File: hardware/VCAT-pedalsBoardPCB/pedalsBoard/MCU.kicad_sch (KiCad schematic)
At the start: 0 parts

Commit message: test
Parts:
- added D1: LED, LHRS_Special:RGB_LED, symbol Device:LED
- added D2, D3: LED, symbol Device:LED
- added R5, R7, R8: 1k, Resistor_SMD:R_0603_1608Metric, symbol Device:R
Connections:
- net 48PinMCU1/PB0: now also R5.1
- net 48PinMCU1/PB1: now also R7.1
- net 48PinMCU1/PB2: now also R8.1
- net GND: now also D1.1 (K), D2.1 (K), D3.1 (K)
- new net: D3.2 (A), R8.2
- new net: D1.2 (A), R5.2
- new net: D2.2 (A), R7.2
- no-connect marks 25 -> 21
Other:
- sheet 48PinMCU1 ports: added none; removed USB_DM, USB_DP

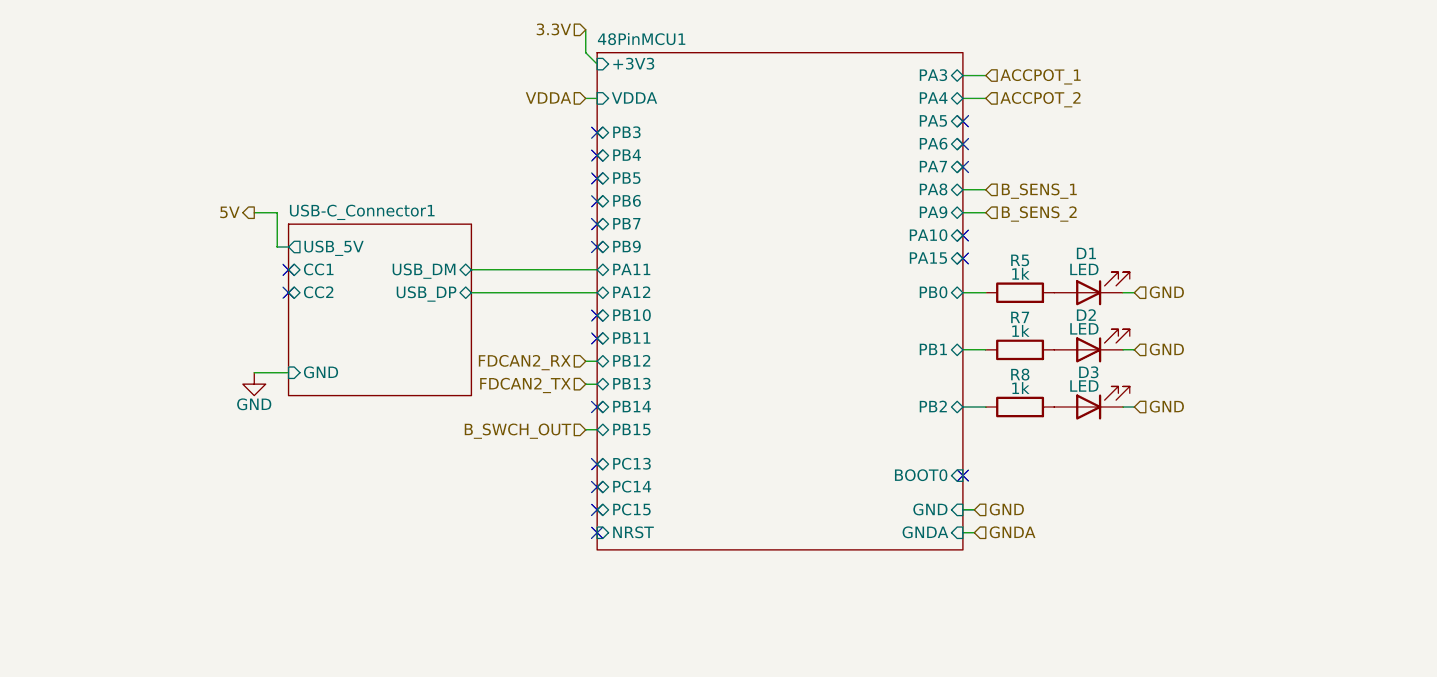
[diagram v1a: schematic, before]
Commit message: implemented review suggestions and added bus
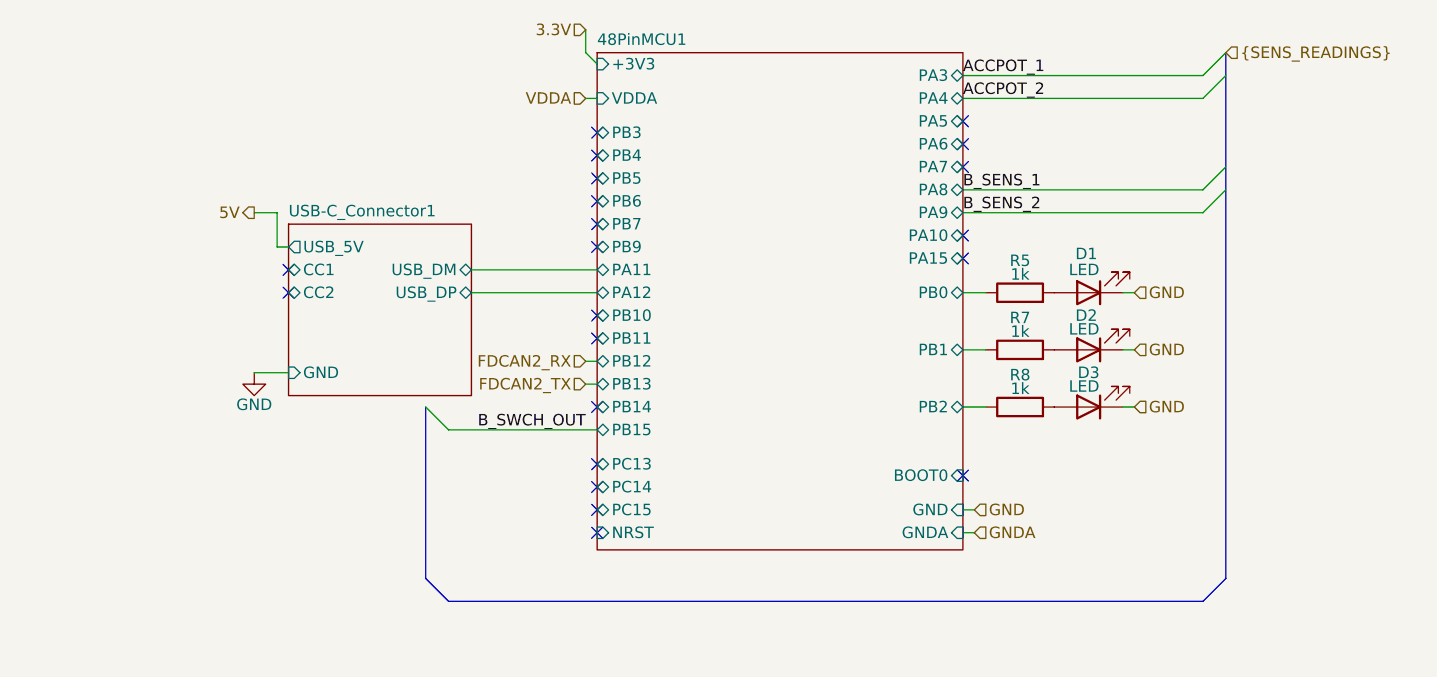
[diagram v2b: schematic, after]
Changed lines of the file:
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@@
 		(at 44.45 64.77)
 	)
-	(wire
-		(pts
-			(xy 119.38 43.18) (xy 121.92 43.18)
+	(bus_entry
+		(at 148.59 53.34)
+		(size -2.54 2.54)
+		(stroke
+			(width 0)
+			(type default)
+		)
+	)
+	(bus_entry
+		(at 59.69 77.47)
+		(size 2.54 2.54)
+		(stroke
+			(width 0)
+			(type default)
+		)
+	)
+	(bus_entry
+		(at 148.59 50.8)
+		(size -2.54 2.54)
+		(stroke
+			(width 0)
+			(type default)
+		)
+	)
+	(bus_entry
+		(at 148.59 38.1)
+		(size -2.54 2.54)
+		(stroke
+			(width 0)
+			(type default)
+		)
+	)
+	(bus_entry
+		(at 148.59 40.64)
+		(size -2.54 2.54)
+		(stroke
+			(width 0)
+			(type default)
+		)
+	)
+	(bus
+		(pts
+			(xy 59.69 77.47) (xy 59.69 96.52)
+		)
+		(stroke
+			(width 0)
+			(type default)
+		)
+	)
+	(wire
+		(pts
+			(xy 119.38 53.34) (xy 146.05 53.34)
+		)
+		(stroke
+			(width 0)
+			(type default)
+		)
+	)
+	(bus
+		(pts
+			(xy 148.59 38.1) (xy 148.59 96.52)
 		)
 		(stroke
@@
 	(wire
 		(pts
+			(xy 119.38 40.64) (xy 146.05 40.64)
+		)
+		(stroke
+			(width 0)
+			(type default)
+		)
+	)
+	(wire
+		(pts
 			(xy 119.38 71.12) (xy 121.92 71.12)
 		)
@@
 	(wire
 		(pts
-			(xy 119.38 40.64) (xy 121.92 40.64)
-		)
-		(stroke
-			(width 0)
-			(type default)
-		)
-	)
-	(wire
-		(pts
-			(xy 77.47 80.01) (xy 78.74 80.01)
+			(xy 119.38 43.18) (xy 146.05 43.18)
 		)
 		(stroke
@@
 		)
 	)
+	(bus
+		(pts
+			(xy 59.69 96.52) (xy 62.23 99.06)
+		)
+		(stroke
+			(width 0)
+			(type default)
+		)
+	)
 	(wire
 		(pts
@@
 		)
 	)
+	(bus
+		(pts
+			(xy 62.23 99.06) (xy 146.05 99.06)
+		)
+		(stroke
+			(width 0)
+			(type default)
+		)
+	)
 	(wire
 		(pts
@@
 	(wire
 		(pts
-			(xy 119.38 53.34) (xy 121.92 53.34)
-		)
-		(stroke
-			(width 0)
-			(type default)
-		)
-	)
-	(wire
-		(pts
 			(xy 137.16 64.77) (xy 138.43 64.77)
 		)
@@
 	(wire
 		(pts
-			(xy 119.38 55.88) (xy 121.92 55.88)
-		)
-		(stroke
-			(width 0)
-			(type default)
+			(xy 62.23 80.01) (xy 78.74 80.01)
+		)
+		(stroke
+			(width 0)
+			(type default)
+		)
+	)
+	(wire
+		(pts
+			(xy 119.38 55.88) (xy 146.05 55.88)
+		)
+		(stroke
+			(width 0)
+			(type default)
+		)
+	)
+	(bus
+		(pts
+			(xy 146.05 99.06) (xy 148.59 96.52)
+		)
+		(stroke
+			(width 0)
+			(type default)
+		)
+	)
+	(label "B_SENS_2"
+		(at 119.38 55.88 0)
+		(effects
+			(font
+				(size 1.27 1.27)
+			)
+			(justify left bottom)
+		)
+	)
+	(label "ACCPOT_1"
+		(at 119.38 40.64 0)
+		(effects
+			(font
+				(size 1.27 1.27)
+			)
+			(justify left bottom)
+		)
+	)
+	(label "ACCPOT_2"
+		(at 119.38 43.18 0)
+		(effects
+			(font
+				(size 1.27 1.27)
+			)
+			(justify left bottom)
+		)
+	)
+	(label "B_SWCH_OUT"
+		(at 77.47 80.01 180)
+		(effects
+			(font
+				(size 1.27 1.27)
+			)
+			(justify right bottom)
+		)
+	)
+	(label "B_SENS_1"
+		(at 119.38 53.34 0)
+		(effects
+			(font
+				(size 1.27 1.27)
+			)
+			(justify left bottom)
 		)
 	)
@@
 			)
 			(justify left)
-		)
-	)
-	(hierarchical_label "B_SWCH_OUT"
-		(shape input)
-		(at 77.47 80.01 180)
-		(effects
-			(font
-				(size 1.27 1.27)
-			)
-			(justify right)
 		)
 	)
@@
 		)
 	)
-	(hierarchical_label "B_SENS_2"
-		(shape input)
-		(at 121.92 55.88 0)
+	(hierarchical_label "FDCAN2_TX"
+		(shape input)
+		(at 77.47 74.93 180)
+		(effects
+			(font
+				(size 1.27 1.27)
+			)
+			(justify right)
+		)
+	)
+	(hierarchical_label "GND"
+		(shape input)
+		(at 138.43 77.47 0)
 		(effects
 			(font
@@
 		)
 	)
-	(hierarchical_label "B_SENS_1"
-		(shape input)
-		(at 121.92 53.34 0)
+	(hierarchical_label "GND"
+		(shape input)
+		(at 138.43 64.77 0)
 		(effects
 			(font
@@
 		)
 	)
-	(hierarchical_label "FDCAN2_TX"
-		(shape input)
-		(at 77.47 74.93 180)
-		(effects
-			(font
-				(size 1.27 1.27)
-			)
-			(justify right)
-		)
-	)
-	(hierarchical_label "ACCPOT_2"
-		(shape input)
-		(at 121.92 43.18 0)
-		(effects
-			(font
-				(size 1.27 1.27)
-			)
-			(justify left)
-		)
-	)
-	(hierarchical_label "GND"
-		(shape input)
-		(at 138.43 77.47 0)
-		(effects
-			(font
-				(size 1.27 1.27)
-			)
-			(justify left)
-		)
-	)
-	(hierarchical_label "GND"
-		(shape input)
-		(at 138.43 64.77 0)
-		(effects
-			(font
-				(size 1.27 1.27)
-			)
-			(justify left)
-		)
-	)
-	(hierarchical_label "ACCPOT_1"
-		(shape input)
-		(at 121.92 40.64 0)
-		(effects
-			(font
+	(hierarchical_label "{SENS_READINGS}"
+		(shape input)
+		(at 148.59 38.1 0)
+		(effects
+			(font
